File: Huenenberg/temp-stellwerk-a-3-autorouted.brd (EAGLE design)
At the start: 99.1 x 61 mm, 120 parts, among them Q1 BSS123, Q10 BSS84, Q11 BSS123, Q12 BSS84, Q13 BSS123, Q14 BSS84, Q15 BSS123, Q16 BSS84, Q17 BSS123, Q18 BSS84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

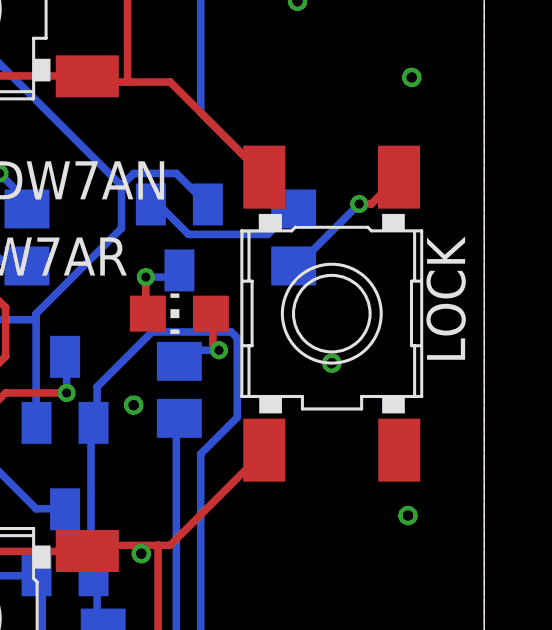
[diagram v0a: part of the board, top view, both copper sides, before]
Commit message: Adds ground planes and vias between ground planes.
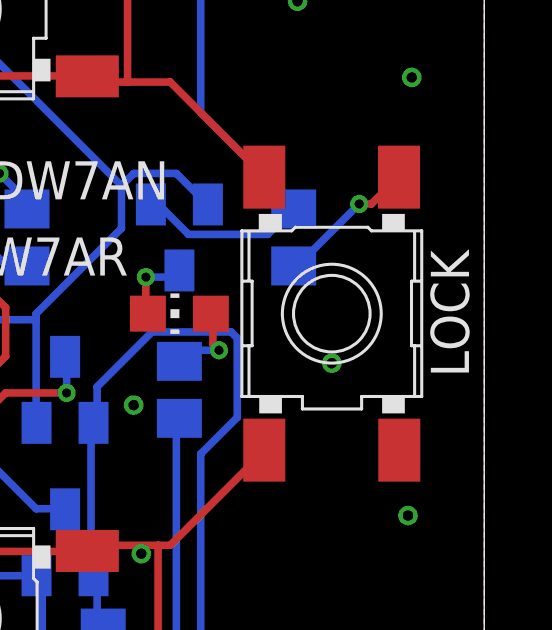
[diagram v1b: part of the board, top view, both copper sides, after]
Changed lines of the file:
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@@
 <setting verticaltext="up"/>
 </settings>
-<grid distance="10" unitdist="mil" unit="mil" style="lines" multiple="1" display="yes" altdistance="5" altunitdist="mil" altunit="mil"/>
+<grid distance="50" unitdist="mil" unit="mil" style="lines" multiple="1" display="yes" altdistance="5" altunitdist="mil" altunit="mil"/>
 <layers>
 <layer number="1" name="Top" color="4" fill="1" visible="yes" active="yes"/>
@@
 <layer number="23" name="tOrigins" color="15" fill="1" visible="yes" active="yes"/>
 <layer number="24" name="bOrigins" color="15" fill="1" visible="no" active="yes"/>
-<layer number="25" name="tNames" color="7" fill="1" visible="yes" active="yes"/>
+<layer number="25" name="tNames" color="7" fill="1" visible="no" active="yes"/>
 <layer number="26" name="bNames" color="7" fill="1" visible="no" active="yes"/>
-<layer number="27" name="tValues" color="7" fill="1" visible="no" active="yes"/>
+<layer number="27" name="tValues" color="7" fill="1" visible="yes" active="yes"/>
 <layer number="28" name="bValues" color="7" fill="1" visible="no" active="yes"/>
 <layer number="29" name="tStop" color="7" fill="3" visible="no" active="yes"/>
@@
 <wire x1="71.12" y1="38.1" x2="69.85" y2="39.37" width="0.254" layer="27"/>
 <wire x1="71.12" y1="38.1" x2="69.85" y2="36.83" width="0.254" layer="27"/>
+<wire x1="82.55" y1="38.1" x2="82.55" y2="36.83" width="0.254" layer="27"/>
+<wire x1="82.55" y1="36.83" x2="85.09" y2="34.29" width="0.254" layer="27"/>
+<wire x1="85.09" y1="34.29" x2="85.09" y2="33.02" width="0.254" layer="27"/>
+<wire x1="85.09" y1="33.02" x2="81.28" y2="33.02" width="0.254" layer="27"/>
+<wire x1="81.28" y1="33.02" x2="82.55" y2="34.29" width="0.254" layer="27"/>
+<wire x1="81.28" y1="33.02" x2="82.55" y2="31.75" width="0.254" layer="27"/>
+<wire x1="82.55" y1="22.86" x2="82.55" y2="24.13" width="0.254" layer="27"/>
+<wire x1="82.55" y1="24.13" x2="85.09" y2="26.67" width="0.254" layer="27"/>
+<wire x1="85.09" y1="26.67" x2="85.09" y2="27.94" width="0.254" layer="27"/>
+<wire x1="85.09" y1="27.94" x2="81.28" y2="27.94" width="0.254" layer="27"/>
+<wire x1="81.28" y1="27.94" x2="82.55" y2="29.21" width="0.254" layer="27"/>
+<wire x1="81.28" y1="27.94" x2="82.55" y2="26.67" width="0.254" layer="27"/>
 </plain>
 <attributes>
@@
 </element>
 <element name="LOCK" library="g-e2e-training" package="TACTSW-6X6" value="LOCK" x="93.98" y="30.48" smashed="yes" rot="R270">
-<attribute name="NAME" x="97.155" y="33.02" size="1.27" layer="25" rot="R270"/>
-<attribute name="VALUE" x="97.155" y="33.02" size="1.27" layer="27" rot="R270"/>
+<attribute name="NAME" x="98.552" y="30.48" size="1.27" layer="25" rot="R270" align="top-center"/>
+<attribute name="VALUE" x="97.155" y="30.48" size="1.27" layer="27" rot="R270" align="bottom-center"/>
 </element>
 <element name="Q1" library="eagleparts" package="SOT23-NCH" value="BSS123" x="71.12" y="27.94" smashed="yes" rot="MR180">
